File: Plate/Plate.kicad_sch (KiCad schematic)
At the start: 8 parts

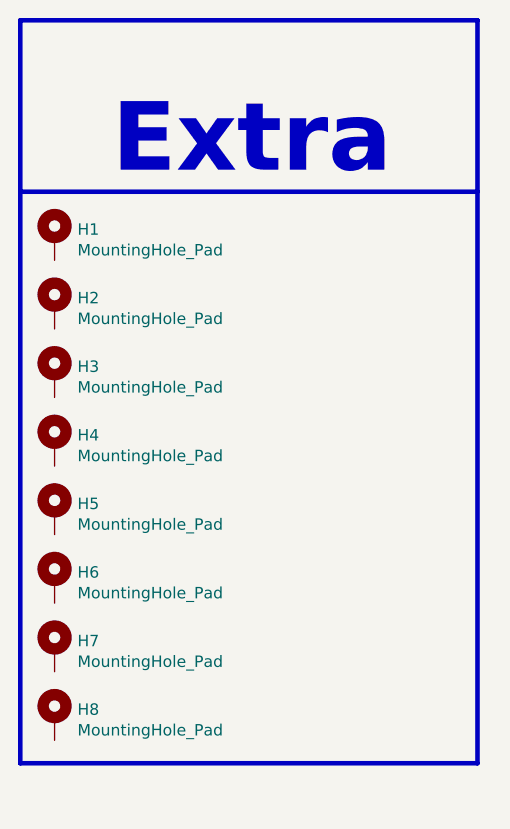
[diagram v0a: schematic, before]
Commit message: Update top offset
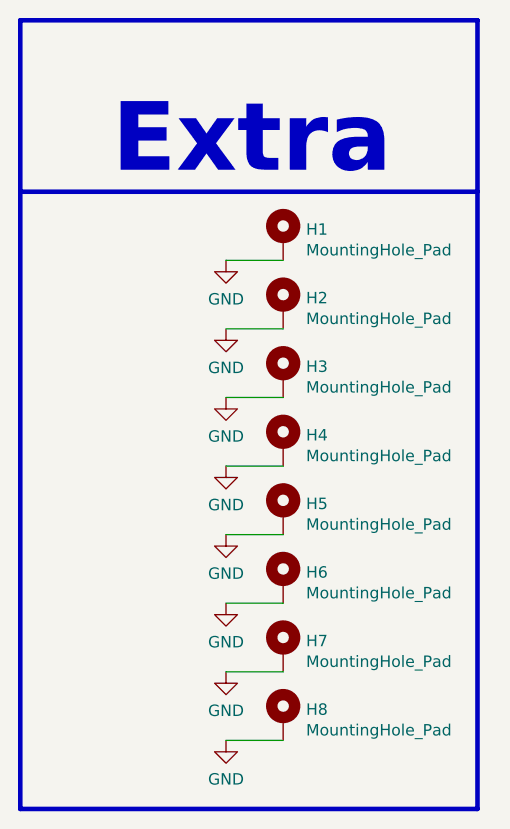
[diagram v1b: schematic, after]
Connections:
- net GND: now reaches H6.1
- net GND: now also H1.1, H2.1, H3.1, H4.1, H5.1, H7.1, H8.1
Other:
- moved on the sheet: H1, H2, H3, H4, H5, H6, H7, H8
